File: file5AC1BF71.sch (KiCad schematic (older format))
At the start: 31 parts

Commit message: Board Design Update RevA
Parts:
- added C_OABY10, C_OABY11, C_OABY12, C_OABY13, C_OABY7, C_OABY8, C_OABY9, C_PWRBY3: 100nF, symbol C
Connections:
- wire segments 161 -> 178
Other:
- note added: "PLL SQUARE/\nRAMP \nSELECTOR \nSWITCH"
- note removed: "PLL SQUARE/RAMP \nSELECTOR SWITCH"
- moved on the sheet: C1_NEG2, C2_NEG2, R_OA_IN1, R_OA_OUT1, R_OA_OUT_F1, R_SAW1, R_SAW2, U_NEG2, U_SAW_OA1A

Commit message: update
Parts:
- C_OABY10, C_OABY11, C_OABY12, C_OABY13, C_OABY7, C_OABY8, C_OABY9, C_PWRBY3: footprint (none) -> Capacitors_SMD:C_0805_HandSoldering
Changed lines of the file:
@@
 F 0 "C_OABY7" V 1875 2500 50  0000 L CNN
 F 1 "100nF" V 1975 2500 50  0000 L CNN
-F 2 "" H 2088 2625 50  0001 C CNN
+F 2 "Capacitors_SMD:C_0805_HandSoldering" H 2088 2625 50  0001 C CNN
 F 3 "" H 2050 2775 50  0001 C CNN
 	1    2050 2775
@@
 F 0 "C_OABY8" V 1875 3150 50  0000 L CNN
 F 1 "100nF" V 1975 3150 50  0000 L CNN
-F 2 "" H 2088 3275 50  0001 C CNN
+F 2 "Capacitors_SMD:C_0805_HandSoldering" H 2088 3275 50  0001 C CNN
 F 3 "" H 2050 3425 50  0001 C CNN
 	1    2050 3425
@@
 F 0 "C_OABY9" V 6425 1025 50  0000 L CNN
 F 1 "100nF" V 6525 1025 50  0000 L CNN
-F 2 "" H 6638 1150 50  0001 C CNN
+F 2 "Capacitors_SMD:C_0805_HandSoldering" H 6638 1150 50  0001 C CNN
 F 3 "" H 6600 1300 50  0001 C CNN
 	1    6600 1300
@@
 F 0 "C_OABY10" V 6525 1725 50  0000 L CNN
 F 1 "100nF" V 6725 1725 50  0000 L CNN
-F 2 "" H 6688 1850 50  0001 C CNN
+F 2 "Capacitors_SMD:C_0805_HandSoldering" H 6688 1850 50  0001 C CNN
 F 3 "" H 6650 2000 50  0001 C CNN
 	1    6650 2000
@@
 F 0 "C_OABY12" V 9725 3100 50  0000 L CNN
 F 1 "100nF" V 9800 3100 50  0000 L CNN
-F 2 "" H 9888 3250 50  0001 C CNN
+F 2 "Capacitors_SMD:C_0805_HandSoldering" H 9888 3250 50  0001 C CNN
 F 3 "" H 9850 3400 50  0001 C CNN
 	1    9850 3400
@@
 F 0 "C_OABY11" V 9600 2075 50  0000 L CNN
 F 1 "100nF" V 9700 2075 50  0000 L CNN
-F 2 "" H 9813 2200 50  0001 C CNN
+F 2 "Capacitors_SMD:C_0805_HandSoldering" H 9813 2200 50  0001 C CNN
 F 3 "" H 9775 2350 50  0001 C CNN
 	1    9775 2350
@@
 F 0 "C_OABY13" V 4800 2550 50  0000 L CNN
 F 1 "100nF" V 4900 2550 50  0000 L CNN
-F 2 "" H 5013 2675 50  0001 C CNN
+F 2 "Capacitors_SMD:C_0805_HandSoldering" H 5013 2675 50  0001 C CNN
 F 3 "" H 4975 2825 50  0001 C CNN
 	1    4975 2825
@@
 F 0 "C_PWRBY3" H 1875 1425 50  0000 L CNN
 F 1 "100nF" H 2025 1525 50  0000 L CNN
-F 2 "" H 1763 1325 50  0001 C CNN
+F 2 "Capacitors_SMD:C_0805_HandSoldering" H 1763 1325 50  0001 C CNN
 F 3 "" H 1725 1475 50  0001 C CNN
 	1    1725 1475

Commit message: Second draft PCB layout
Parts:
- added R_SAWJOIN1: 10R, Resistors_SMD:R_0805_HandSoldering, symbol R
- added R_SWING1: 22K, Resistors_SMD:R_0805_HandSoldering, symbol R
- renumbered C_SAW1 to C_SAWINT1, R_SAW2 to R_SAWFB1
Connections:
- wire segments 178 -> 184
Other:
- note added: "FREQUENCY\nMOD B50K POT"
- note added: "PLL DAMPEN\nCONTROL \nB100K POT"
- note added: "PLL INPUT\nTRIGGER \nB10K POT\n"
- note added: "PLL SAMPLE AND\nHOLD SEL \nSPDT SWITCH"
- note added: "PLL SQUARE/\nRAMP \nSELECTOR \nSPDT SWITCH"
- note added: "PLL SWING\nCONTROL \nB1M POT"
- note removed: "FREQUENCY\nMOD POT"
- note removed: "PLL DAMPEN\nCONTROL POT"
- note removed: "PLL INPUT\nTRIGGER POT\n"
- note removed: "PLL SAMPLE AND\nHOLD SEL SWITCH"
- note removed: "PLL SQUARE/\nRAMP \nSELECTOR \nSWITCH"
- note removed: "PLL SWING\nCONTROL POT"
- moved on the sheet: C1_NEG2, C2_NEG2, C_OABY10, C_OABY11, C_OABY12, C_OABY13, C_OABY7, C_OABY9, C_PWRBY3, C_SAWINT1, R_OA_OUT1, R_OA_OUT_F1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

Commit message: Corrections to board dimensions, adjusted layout to fit
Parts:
- removed C_SH1: 100nF, Capacitors_SMD:C_0805_HandSoldering, symbol C
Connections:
- wire segments 184 -> 183
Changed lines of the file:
@@
-$EndComp
-$Comp
-L C C_SH1
-U 1 1 5AC1C6CB
-P 6575 4375
-F 0 "C_SH1" H 6600 4475 50  0000 L CNN
-F 1 "100nF" H 6600 4275 50  0000 L CNN
-F 2 "Capacitors_SMD:C_0805_HandSoldering" H 6613 4225 50  0001 C CNN
-F 3 "" H 6575 4375 50  0001 C CNN
-	1    6575 4375
-	1    0    0    -1
 $EndComp
 $Comp
@@
 Text HLabel 5200 4350 3    60   Input ~ 0
 GND
-Text HLabel 6575 4950 3    60   Input ~ 0
-GND
 Text HLabel 7625 5800 3    60   Input ~ 0
 GND
@@
 Wire Wire Line
 	10400 2125 10400 2575
-Wire Wire Line
-	6575 4525 6575 4950
-Wire Wire Line
-	6575 3475 6575 4225
 Connection ~ 7625 4900
 Wire Wire Line
@@
 Wire Wire Line
 	7400 4900 9200 4900
-Wire Wire Line
-	7625 4125 6575 4125
 Wire Wire Line
 	3950 3675 3950 3950
@@
 Wire Wire Line
 	6575 3475 5900 3475
-Connection ~ 6575 4125
 Wire Wire Line
 	9200 4900 9200 4950
@@
 Text Notes 7550 3550 0    39   ~ 0
 PLL SWING\nCONTROL \nB1M POT
-Text Notes 7550 4600 0    39   ~ 0
+Text Notes 7550 4625 0    39   ~ 0
 PLL DAMPEN\nCONTROL \nB100K POT
 Text Label 8850 2875 1    39   ~ 0
@@
 	0    1    1    0
 $EndComp
+Wire Wire Line
+	6575 3475 6575 4125
+Wire Wire Line
+	6575 4125 7625 4125
 $EndSCHEMATC

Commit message: layout update
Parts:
- removed C_OABY10, C_OABY11, C_OABY12, C_OABY9: 100nF, Capacitors_SMD:C_0805_HandSoldering, symbol C
- removed U_OAFX_IN1, U_OAFX_OUT1: _TL071, SMD_Packages:SOIC-8-N, symbol _TL071
- removed U_SAW_OA1: _TL072, SMD_Packages:SOIC-8-N, symbol _TL072
- added U_OAFX1: TL074, SMD_Packages:SOIC-14_N, symbol TL074
- renumbered C_OABY7 to C_OABY3, C_OABY8 to C_OABY4
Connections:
- wire segments 183 -> 171
- no-connect marks 11 -> 7
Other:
- moved on the sheet: C_OABY4
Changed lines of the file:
@@
 	1    0    0    -1
 $EndComp
-NoConn ~ 2425 3375
-NoConn ~ 2525 3375
 NoConn ~ 5900 3875
-$Comp
-L _TL071 U_OAFX_IN1
-U 1 1 5AC1C6A3
-P 2425 3075
-F 0 "U_OAFX_IN1" H 2425 3325 50  0000 L CNN
-F 1 "_TL071" H 2425 3225 50  0000 L CNN
-F 2 "SMD_Packages:SOIC-8-N" H 2475 3125 50  0001 C CNN
-F 3 "" H 2575 3225 50  0001 C CNN
-	1    2425 3075
-	1    0    0    -1
-$EndComp
 $Comp
 L NPOT SWING1
@@
 	0    -1   -1   0
 $EndComp
-$Comp
-L _TL071 U_OAFX_OUT1
-U 1 1 5AC1C6D7
-P 10500 2875
-F 0 "U_OAFX_OUT1" H 10500 3125 50  0000 L CNN
-F 1 "_TL071" H 10500 3025 50  0000 L CNN
-F 2 "SMD_Packages:SOIC-8-N" H 10550 2925 50  0001 C CNN
-F 3 "" H 10650 3025 50  0001 C CNN
-	1    10500 2875
-	1    0    0    -1
-$EndComp
-NoConn ~ 10500 3175
-NoConn ~ 10600 3175
 Text Notes 3550 2875 0    47   ~ 0
 Smaller value \n= more sustain
@@
 Text Label 2325 3625 3    60   ~ 0
 -9V
-$Comp
-L _TL072 U_SAW_OA1
-U 1 1 5AC48A64
-P 6950 1525
-F 0 "U_SAW_OA1" H 6950 1775 50  0000 L CNN
-F 1 "_TL072" H 6975 1700 50  0000 L CNN
-F 2 "SMD_Packages:SOIC-8-N" H 6950 1525 50  0001 C CNN
-F 3 "" H 6950 1525 50  0001 C CNN
-	1    6950 1525
-	1    0    0    -1
-$EndComp
-$Comp
-L _TL072 U_SAW_OA1
-U 2 1 5AC48DD7
-P 8225 1425
-F 0 "U_SAW_OA1" H 8225 1675 50  0000 L CNN
-F 1 "_TL072" H 8250 1600 50  0000 L CNN
-F 2 "SMD_Packages:SOIC-8-N" H 8225 1425 50  0001 C CNN
-F 3 "" H 8225 1425 50  0001 C CNN
-	2    8225 1425
-	1    0    0    -1
-$EndComp
 $Comp
 L CP C_HOLD2
@@
 PLL SQUARE/\nRAMP \nSELECTOR \nSPDT SWITCH
 $Comp
-L C C_OABY7
+L C C_OABY3
 U 1 1 5AC4BA5A
 P 2050 2575
-F 0 "C_OABY7" V 1875 2300 50  0000 L CNN
+F 0 "C_OABY3" V 1875 2300 50  0000 L CNN
 F 1 "100nF" V 1975 2300 50  0000 L CNN
 F 2 "Capacitors_SMD:C_0805_HandSoldering" H 2088 2425 50  0001 C CNN
@@
 GND
 $Comp
-L C C_OABY8
+L C C_OABY4
 U 1 1 5AC4C7DB
-P 2050 3425
-F 0 "C_OABY8" V 1875 3150 50  0000 L CNN
-F 1 "100nF" V 1975 3150 50  0000 L CNN
-F 2 "Capacitors_SMD:C_0805_HandSoldering" H 2088 3275 50  0001 C CNN
-F 3 "" H 2050 3425 50  0001 C CNN
-	1    2050 3425
+P 2050 3500
+F 0 "C_OABY4" V 1875 3225 50  0000 L CNN
+F 1 "100nF" V 1975 3225 50  0000 L CNN
+F 2 "Capacitors_SMD:C_0805_HandSoldering" H 2088 3350 50  0001 C CNN
+F 3 "" H 2050 3500 50  0001 C CNN
+	1    2050 3500
 	0    1    1    0
 $EndComp
 Text HLabel 1775 3600 3    60   Input ~ 0
-GND
-$Comp
-L C C_OABY9
-U 1 1 5AC4DFB8
-P 6600 975
-F 0 "C_OABY9" V 6425 700 50  0000 L CNN
-F 1 "100nF" V 6525 700 50  0000 L CNN
-F 2 "Capacitors_SMD:C_0805_HandSoldering" H 6638 825 50  0001 C CNN
-F 3 "" H 6600 975 50  0001 C CNN
-	1    6600 975
-	0    1    1    0
-$EndComp
-Text HLabel 6325 1075 3    60   Input ~ 0
-GND
-$Comp
-L C C_OABY10
-U 1 1 5AC4EE84
-P 6650 1825
-F 0 "C_OABY10" V 6525 1550 50  0000 L CNN
-F 1 "100nF" V 6725 1550 50  0000 L CNN
-F 2 "Capacitors_SMD:C_0805_HandSoldering" H 6688 1675 50  0001 C CNN
-F 3 "" H 6650 1825 50  0001 C CNN
-	1    6650 1825
-	0    1    1    0
-$EndComp
-Text HLabel 6300 1925 3    60   Input ~ 0
-GND
-$Comp
-L C C_OABY12
-U 1 1 5AC50D51
-P 10200 3400
-F 0 "C_OABY12" V 10075 3100 50  0000 L CNN
-F 1 "100nF" V 10150 3100 50  0000 L CNN
-F 2 "Capacitors_SMD:C_0805_HandSoldering" H 10238 3250 50  0001 C CNN
-F 3 "" H 10200 3400 50  0001 C CNN
-	1    10200 3400
-	0    1    1    0
-$EndComp
-Text HLabel 10000 3500 3    60   Input ~ 0
-GND
-$Comp
-L C C_OABY11
-U 1 1 5AC516B4
-P 10125 2350
-F 0 "C_OABY11" V 9950 2075 50  0000 L CNN
-F 1 "100nF" V 10050 2075 50  0000 L CNN
-F 2 "Capacitors_SMD:C_0805_HandSoldering" H 10163 2200 50  0001 C CNN
-F 3 "" H 10125 2350 50  0001 C CNN
-	1    10125 2350
-	0    1    1    0
-$EndComp
-Text HLabel 9700 2425 3    60   Input ~ 0
 GND
 $Comp
@@
 Wire Wire Line
 	9750 2975 9750 3850
-Wire Wire Line
-	10400 3175 10400 3550
-Wire Wire Line
-	10400 2125 10400 2575
 Connection ~ 7625 4900
 Wire Wire Line
@@
 Connection ~ 8625 1425
 Wire Wire Line
-	6850 800  6850 1225
-Wire Wire Line
 	8125 1875 8125 1725
 Wire Wire Line
@@
 	1775 2575 1900 2575
 Wire Wire Line
-	1775 3425 1900 3425
-Wire Wire Line
-	2200 3425 2325 3425
-Connection ~ 2325 3425
-Wire Wire Line
-	1775 3600 1775 3425
-Wire Wire Line
-	6325 975  6450 975
-Wire Wire Line
-	6750 975  6850 975
-Connection ~ 6850 975
-Wire Wire Line
-	6300 1825 6500 1825
-Wire Wire Line
-	6850 1825 6800 1825
-Wire Wire Line
-	10000 3500 10000 3400
-Wire Wire Line
-	10000 3400 10050 3400
-Wire Wire Line
-	9700 2350 9975 2350
-Wire Wire Line
-	10350 3400 10400 3400
-Connection ~ 10400 3400
-Wire Wire Line
-	10275 2350 10400 2350
-Connection ~ 10400 2350
+	1775 3500 1900 3500
+Wire Wire Line
+	2200 3500 2325 3500
+Connection ~ 2325 3500
+Wire Wire Line
+	1775 3600 1775 3500
 Wire Wire Line
 	4700 2575 4825 2575
@@
 	4700 2575 4700 2625
 Wire Wire Line
-	6325 975  6325 1075
-Wire Wire Line
-	9700 2425 9700 2350
-Wire Wire Line
 	5900 3275 6450 3275
 Wire Wire Line
 	6750 3275 7625 3275
 Wire Wire Line
-	6300 1825 6300 1925
-Wire Wire Line
 	6575 3475 6575 4125
 Wire Wire Line
 	6575 4125 7625 4125
+$Comp
+L TL074 U_OAFX1
+U 1 1 5ACA100A
+P 10500 2875
+F 0 "U_OAFX1" H 10500 3075 50  0000 L CNN
+F 1 "TL074" H 10500 2675 50  0000 L CNN
+F 2 "SMD_Packages:SOIC-14_N" H 10450 2975 50  0001 C CNN
+F 3 "" H 10550 3075 50  0001 C CNN
+	1    10500 2875
+	1    0    0    -1
+$EndComp
+$Comp
+L TL074 U_OAFX1
+U 2 1 5ACA12C9
+P 6950 1525
+F 0 "U_OAFX1" H 6950 1725 50  0000 L CNN
+F 1 "TL074" H 6950 1325 50  0000 L CNN
+F 2 "SMD_Packages:SOIC-14_N" H 6900 1625 50  0001 C CNN
+F 3 "" H 7000 1725 50  0001 C CNN
+	2    6950 1525
+	1    0    0    -1
+$EndComp
+$Comp
+L TL074 U_OAFX1
+U 3 1 5ACA1440
+P 8225 1425
+F 0 "U_OAFX1" H 8225 1625 50  0000 L CNN
+F 1 "TL074" H 8225 1225 50  0000 L CNN
+F 2 "SMD_Packages:SOIC-14_N" H 8175 1525 50  0001 C CNN
+F 3 "" H 8275 1625 50  0001 C CNN
+	3    8225 1425
+	1    0    0    -1
+$EndComp
+$Comp
+L TL074 U_OAFX1
+U 4 1 5ACA1684
+P 2425 3075
+F 0 "U_OAFX1" H 2425 3275 50  0000 L CNN
+F 1 "TL074" H 2425 2875 50  0000 L CNN
+F 2 "SMD_Packages:SOIC-14_N" H 2375 3175 50  0001 C CNN
+F 3 "" H 2475 3275 50  0001 C CNN
+	4    2425 3075
+	1    0    0    -1
+$EndComp
+Wire Wire Line
+	6850 800  6850 1225
+Wire Wire Line
+	10400 2575 10400 2125
+Wire Wire Line
+	10400 3550 10400 3175
 $EndSCHEMATC

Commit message: update
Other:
- note added: "PLL SAMPLE AND\nHOLD SEL \nSPDT SWITCH\nON-OFF-ON"
- note added: "PLL SQUARE/\nRAMP \nSELECTOR \nSPDT SWITCH\nON-ON\n"
- note removed: "PLL SAMPLE AND\nHOLD SEL \nSPDT SWITCH"
- note removed: "PLL SQUARE/\nRAMP \nSELECTOR \nSPDT SWITCH"
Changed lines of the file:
@@
 HOLDSEL_P3
 Text Notes 8550 5650 0    39   ~ 0
-PLL SAMPLE AND\nHOLD SEL \nSPDT SWITCH
+PLL SAMPLE AND\nHOLD SEL \nSPDT SWITCH\nON-OFF-ON
 Text Notes 8575 3150 0    39   ~ 0
-PLL SQUARE/\nRAMP \nSELECTOR \nSPDT SWITCH
+PLL SQUARE/\nRAMP \nSELECTOR \nSPDT SWITCH\nON-ON\n
 $Comp
 L C C_OABY3

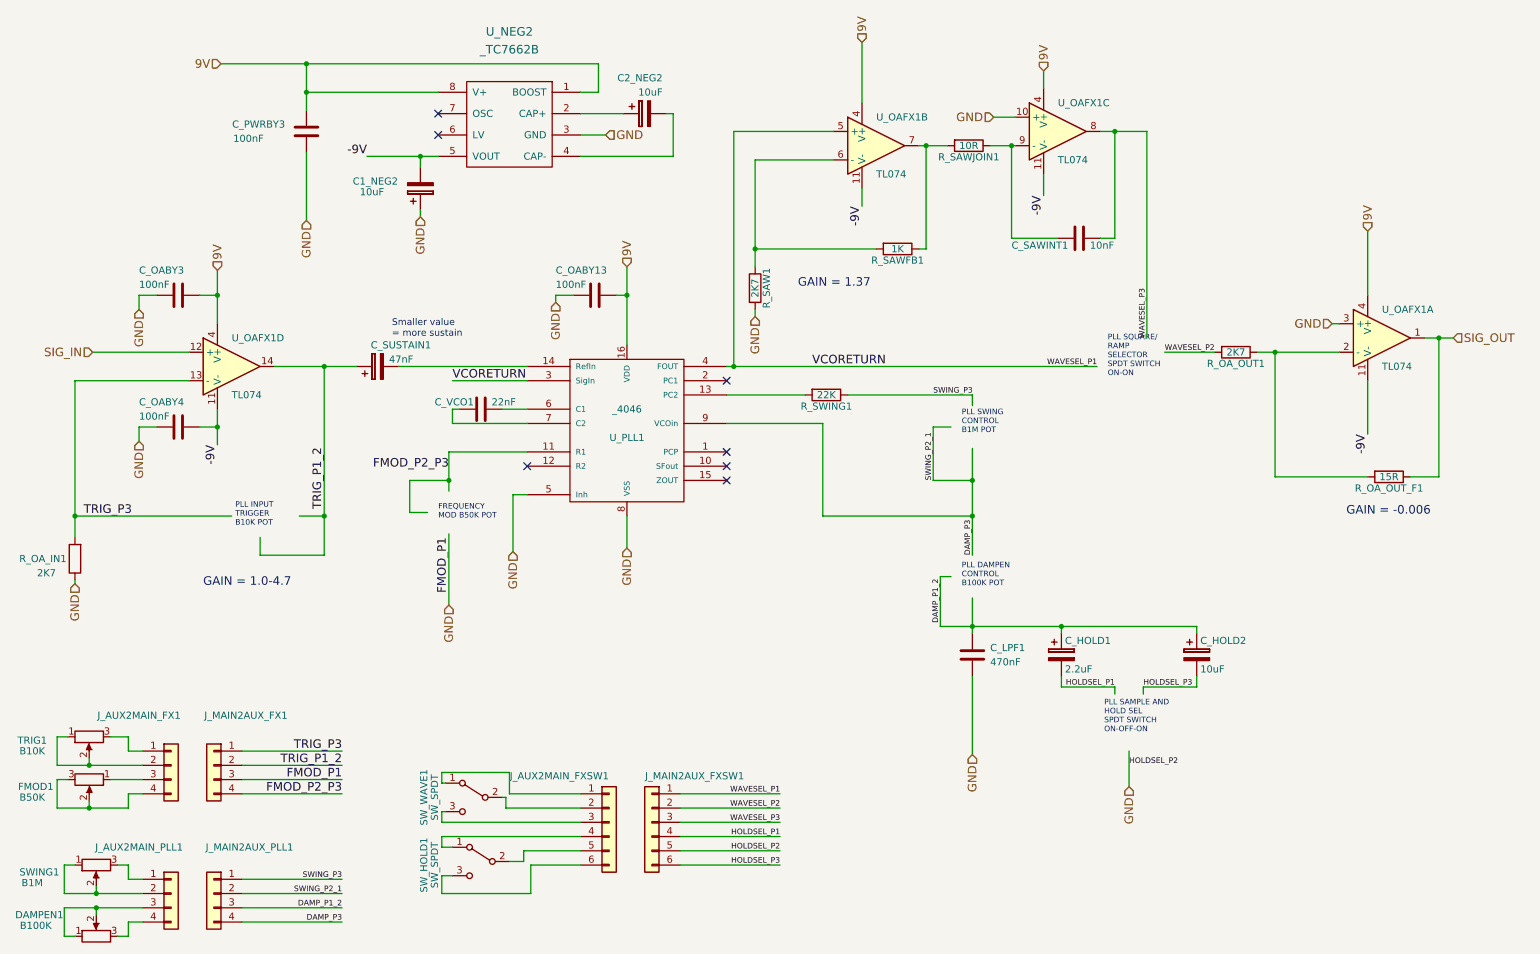
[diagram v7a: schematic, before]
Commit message: Board Layout updates
- Increased PLL footprint width
- Separated FX TL074 into 2 TL072's.
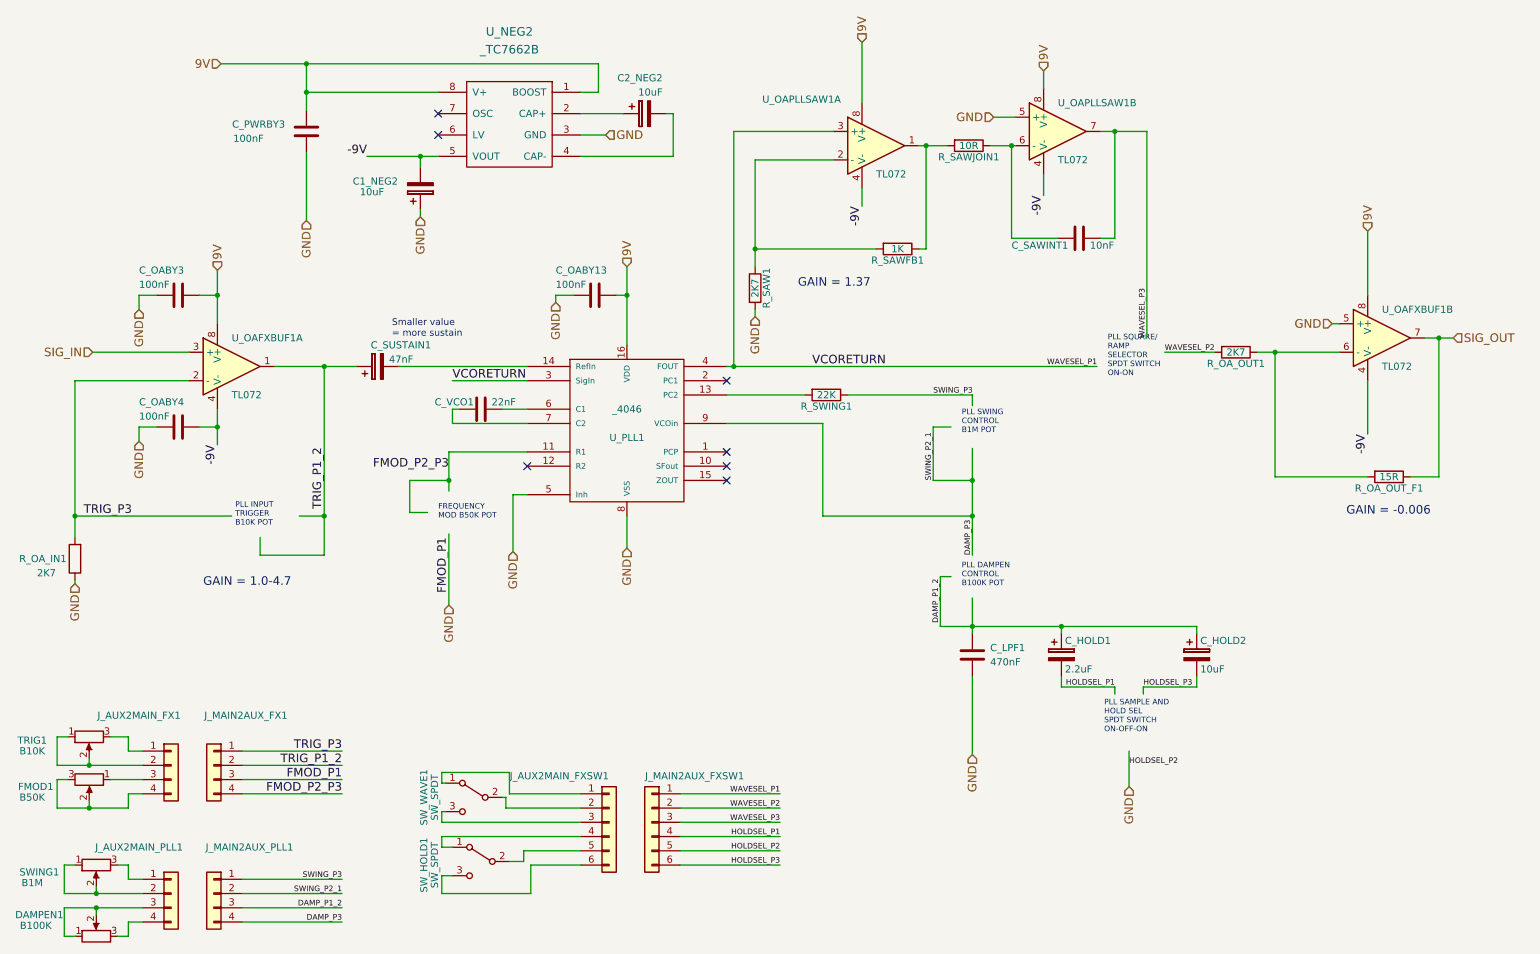
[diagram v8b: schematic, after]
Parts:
- removed U_OAFX1: TL074, SMD_Packages:SOIC-14_N, symbol TL074
- added U_OAFXBUF1, U_OAPLLSAW1: TL072, SMD_Packages:SOIC-8-N, symbol TL072
- U_PLL1: footprint SMD_Packages:SO-16-N -> Custom_SMD_Packages:SO-16-N++
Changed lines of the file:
@@
 F 0 "U_PLL1" H 5200 3375 50  0000 C CNN
 F 1 "_4046" H 5200 3575 50  0000 C CNN
-F 2 "SMD_Packages:SO-16-N" H 5200 3475 60  0001 C CNN
+F 2 "Custom_SMD_Packages:SO-16-N++" H 5200 3475 60  0001 C CNN
 F 3 "" H 5200 3475 60  0001 C CNN
 	1    5200 3475
@@
 Wire Wire Line
 	6575 4125 7625 4125
-$Comp
-L TL074 U_OAFX1
-U 1 1 5ACA100A
+Wire Wire Line
+	6850 800  6850 1225
+Wire Wire Line
+	10400 2575 10400 2125
+Wire Wire Line
+	10400 3550 10400 3175
+$Comp
+L TL072 U_OAPLLSAW1
+U 1 1 5AED44F4
+P 6950 1525
+F 0 "U_OAPLLSAW1" H 6150 1850 50  0000 L CNN
+F 1 "TL072" H 6950 1325 50  0000 L CNN
+F 2 "SMD_Packages:SOIC-8-N" H 6950 1525 50  0001 C CNN
+F 3 "" H 6950 1525 50  0001 C CNN
+	1    6950 1525
+	1    0    0    -1
+$EndComp
+$Comp
+L TL072 U_OAPLLSAW1
+U 2 1 5AED459D
+P 8225 1425
+F 0 "U_OAPLLSAW1" H 8225 1625 50  0000 L CNN
+F 1 "TL072" H 8225 1225 50  0000 L CNN
+F 2 "SMD_Packages:SOIC-8-N" H 8225 1425 50  0001 C CNN
+F 3 "" H 8225 1425 50  0001 C CNN
+	2    8225 1425
+	1    0    0    -1
+$EndComp
+$Comp
+L TL072 U_OAFXBUF1
+U 1 1 5AED4BDA
+P 2425 3075
+F 0 "U_OAFXBUF1" H 2425 3275 50  0000 L CNN
+F 1 "TL072" H 2425 2875 50  0000 L CNN
+F 2 "SMD_Packages:SOIC-8-N" H 2425 3075 50  0001 C CNN
+F 3 "" H 2425 3075 50  0001 C CNN
+	1    2425 3075
+	1    0    0    -1
+$EndComp
+$Comp
+L TL072 U_OAFXBUF1
+U 2 1 5AED53CF
 P 10500 2875
-F 0 "U_OAFX1" H 10500 3075 50  0000 L CNN
-F 1 "TL074" H 10500 2675 50  0000 L CNN
-F 2 "SMD_Packages:SOIC-14_N" H 10450 2975 50  0001 C CNN
-F 3 "" H 10550 3075 50  0001 C CNN
-	1    10500 2875
-	1    0    0    -1
-$EndComp
-$Comp
-L TL074 U_OAFX1
-U 2 1 5ACA12C9
-P 6950 1525
-F 0 "U_OAFX1" H 6950 1725 50  0000 L CNN
-F 1 "TL074" H 6950 1325 50  0000 L CNN
-F 2 "SMD_Packages:SOIC-14_N" H 6900 1625 50  0001 C CNN
-F 3 "" H 7000 1725 50  0001 C CNN
-	2    6950 1525
-	1    0    0    -1
-$EndComp
-$Comp
-L TL074 U_OAFX1
-U 3 1 5ACA1440
-P 8225 1425
-F 0 "U_OAFX1" H 8225 1625 50  0000 L CNN
-F 1 "TL074" H 8225 1225 50  0000 L CNN
-F 2 "SMD_Packages:SOIC-14_N" H 8175 1525 50  0001 C CNN
-F 3 "" H 8275 1625 50  0001 C CNN
-	3    8225 1425
-	1    0    0    -1
-$EndComp
-$Comp
-L TL074 U_OAFX1
-U 4 1 5ACA1684
-P 2425 3075
-F 0 "U_OAFX1" H 2425 3275 50  0000 L CNN
-F 1 "TL074" H 2425 2875 50  0000 L CNN
-F 2 "SMD_Packages:SOIC-14_N" H 2375 3175 50  0001 C CNN
-F 3 "" H 2475 3275 50  0001 C CNN
-	4    2425 3075
-	1    0    0    -1
-$EndComp
-Wire Wire Line
-	6850 800  6850 1225
-Wire Wire Line
-	10400 2575 10400 2125
-Wire Wire Line
-	10400 3550 10400 3175
+F 0 "U_OAFXBUF1" H 10500 3075 50  0000 L CNN
+F 1 "TL072" H 10500 2675 50  0000 L CNN
+F 2 "SMD_Packages:SOIC-8-N" H 10500 2875 50  0001 C CNN
+F 3 "" H 10500 2875 50  0001 C CNN
+	2    10500 2875
+	1    0    0    -1
+$EndComp
 $EndSCHEMATC
